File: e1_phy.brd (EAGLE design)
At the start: 100 x 75 mm, 126 parts, among them IC2 LD117AS33TR, IC3 LD117AS33TR, IC4 MCP4725, U1 IDT82V2081, U2 GPS_GNS_2201, U3 VCTCXO-CONNORWINFIELD, U4 VCXO_TAITIEN_VT, U5 IP4234CZ6, X2 SMA-142-0701-801/806, X3 JACK2.5_SJ-2523, X4 0446200002

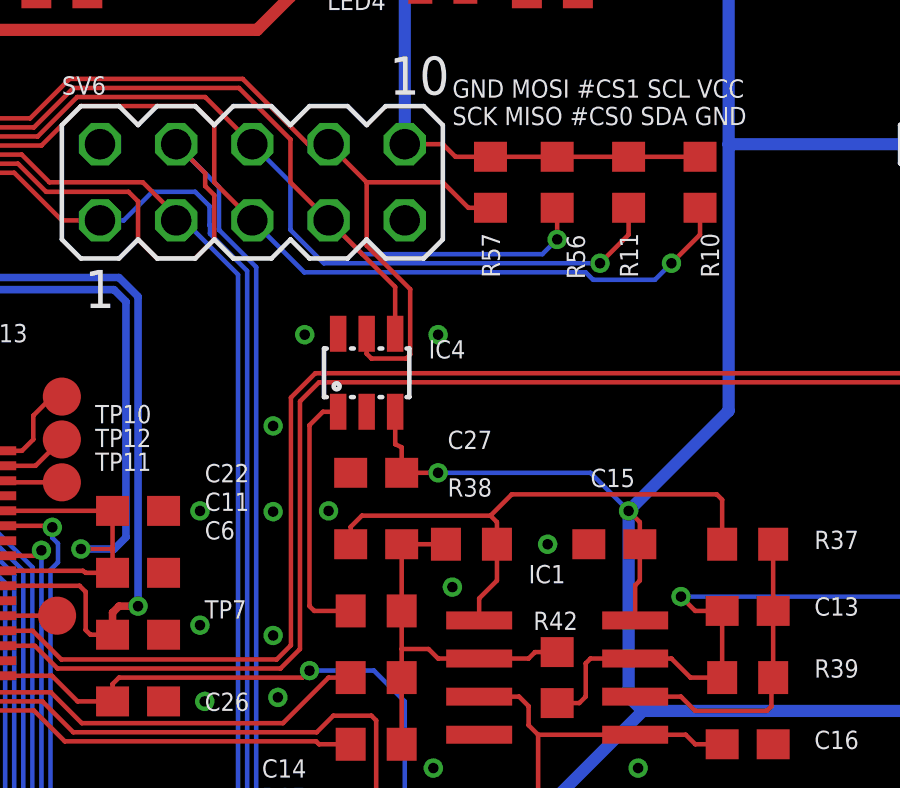
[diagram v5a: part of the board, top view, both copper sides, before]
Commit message: Implement review comments: Switch DAC to Maxim part.
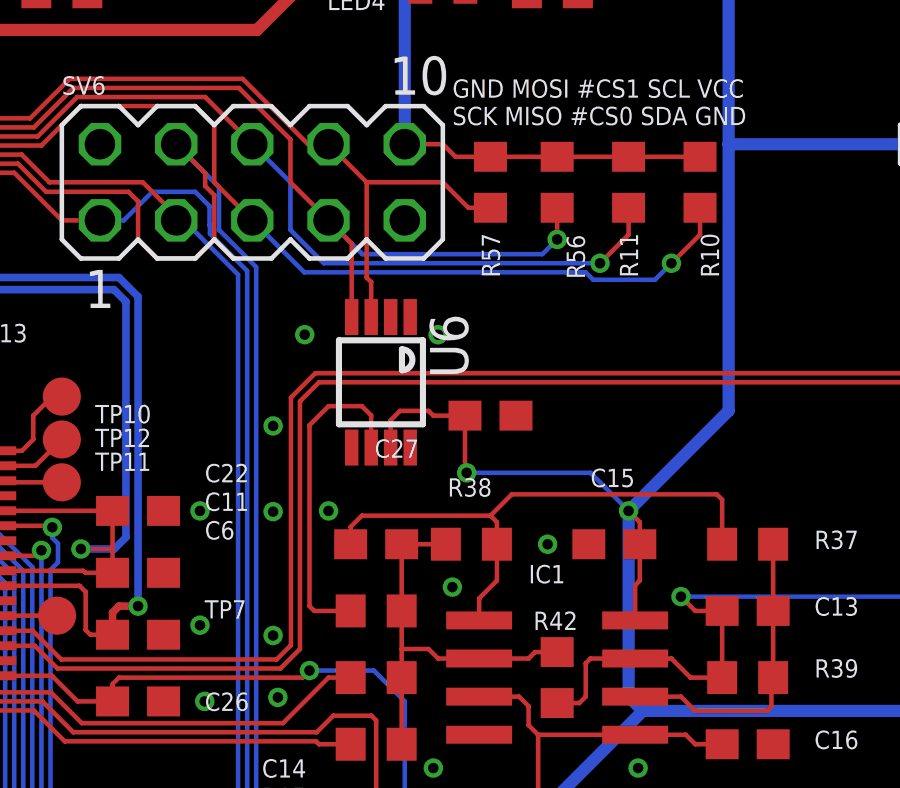
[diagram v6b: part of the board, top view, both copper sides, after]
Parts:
- removed IC4: MCP4725, dp_devices:SOT-23-6
- added U6: (no value), max5215_max5217:UMAX8
- moved C27 4.26 mm to (58.7, 44.3), turned to 180 degrees
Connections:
- net +UB: now also U6.1, U6.7; no longer IC4.3
- net DAC_I2C: now also U6.6; no longer IC4.1
- net GND: now also U6.8; no longer IC4.2, IC4.6
- net I2C_SCL: now also U6.3; no longer IC4.5
- net I2C_SDA: now also U6.4; no longer IC4.4
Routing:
- net I2C_SCL: track 53.9 -> 49.9 mm
- net DAC_I2C: track 8.61 -> 11.0 mm
- net I2C_SDA: track 59.1 -> 57.6 mm
- net +UB: track 197.5 -> 198.7 mm
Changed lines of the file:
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@@
 <attribute name="VALUE" x="25.0825" y="40.8305" size="0.0254" layer="27"/>
 </element>
-<element name="IC4" library="dp_devices" package="SOT-23-6" value="MCP4725" x="54.61" y="45.72" smashed="yes">
-<attribute name="NAME" x="56.67375" y="46.19625" size="0.6096" layer="25" font="vector" ratio="10"/>
-<attribute name="VALUE" x="53.34" y="42.2275" size="1.27" layer="27" font="vector" ratio="10"/>
-</element>
-<element name="C27" library="rcl" package="C0603" value="100n" x="54.9275" y="42.38625" smashed="yes">
-<attribute name="NAME" x="57.30875" y="43.18" size="0.6096" layer="25" font="vector"/>
-<attribute name="VALUE" x="54.2925" y="40.48125" size="1.27" layer="27"/>
+<element name="C27" library="rcl" package="C0603" value="100n" x="58.7375" y="44.29125" smashed="yes" rot="R180">
+<attribute name="NAME" x="56.35625" y="43.4975" size="0.6096" layer="25" font="vector" rot="R180"/>
+<attribute name="VALUE" x="59.3725" y="46.19625" size="1.27" layer="27" rot="R180"/>
 </element>
 <element name="R15" library="rcl" package="R0603" value="10k" x="54.9275" y="37.7825" smashed="yes">
@@
 <attribute name="OC_NEWARK" value="unknown" x="65.56375" y="22.86" size="1.778" layer="27" rot="R180" display="off"/>
 </element>
+<element name="U6" library="max5215_max5217" package="UMAX8" value="" x="55.08625" y="45.4025" rot="R180"/>
 </elements>
 <signals>
@@
 <via x="35.08375" y="39.6875" extent="1-16" drill="0.35"/>
 <contactref element="C27" pad="1"/>
-<contactref element="IC4" pad="2"/>
-<contactref element="IC4" pad="6"/>
 <contactref element="C28" pad="1"/>
 <contactref element="SV5" pad="1"/>
@@
 <contactref element="RN2" pad="4"/>
 <contactref element="RN1" pad="8"/>
+<contactref element="U6" pad="8"/>
 </signal>
 <signal name="LINE_PIN1">
@@
 <wire x1="49.2125" y1="62.865" x2="65.080875" y2="62.865" width="0.4064" layer="16"/>
 <contactref element="C27" pad="2"/>
-<contactref element="IC4" pad="3"/>
 <wire x1="63.715" y1="38.79125" x2="63.715" y2="40.005" width="0.1524" layer="1"/>
 <wire x1="63.56" y1="37.465" x2="63.56" y2="38.63625" width="0.1524" layer="1"/>
@@
 <wire x1="66.675" y1="62.540875" x2="66.675" y2="53.34" width="0.4064" layer="16"/>
 <wire x1="66.675" y1="53.34" x2="66.675" y2="44.45" width="0.4064" layer="16"/>
-<wire x1="55.56" y1="44.42" x2="55.5625" y2="44.4175" width="0.1524" layer="1"/>
-<wire x1="55.5625" y1="43.33875" x2="55.5625" y2="44.4175" width="0.1524" layer="1"/>
-<wire x1="55.7775" y1="42.38625" x2="55.7775" y2="43.23625" width="0.1524" layer="1"/>
-<wire x1="55.7775" y1="43.23625" x2="55.5625" y2="43.33875" width="0.1524" layer="1"/>
 <wire x1="84.24" y1="35.56" x2="84.24" y2="34.71" width="0.1524" layer="1"/>
 <wire x1="84.24" y1="34.71" x2="84.1375" y2="34.44875" width="0.1524" layer="1"/>
@@
 <contactref element="SV5" pad="5"/>
 <wire x1="73.66" y1="53.34" x2="66.675" y2="53.34" width="0.4064" layer="16"/>
-<wire x1="55.7775" y1="42.38625" x2="56.99125" y2="42.38625" width="0.1524" layer="1"/>
-<via x="56.99125" y="42.38625" extent="1-16" drill="0.35"/>
-<wire x1="56.99125" y1="42.38625" x2="62.07125" y2="42.38625" width="0.1524" layer="16"/>
 <wire x1="62.07125" y1="42.38625" x2="63.34125" y2="41.11625" width="0.1524" layer="16"/>
 <contactref element="U1" pad="42"/>
@@
 <wire x1="74.29105" y1="6.54890625" x2="74.29105" y2="14.3925875" width="0.254" layer="16"/>
 <wire x1="74.16925" y1="14.5143875" x2="74.16925" y2="33.21175" width="0.254" layer="16"/>
+<contactref element="U6" pad="7"/>
+<contactref element="U6" pad="1"/>
+<wire x1="55.41125" y1="43.2275" x2="55.41125" y2="44.14" width="0.1524" layer="1"/>
+<wire x1="55.72125" y1="44.45" x2="55.41125" y2="44.14" width="0.1524" layer="1"/>
+<wire x1="57.8875" y1="44.29125" x2="56.8325" y2="44.29125" width="0.1524" layer="1"/>
+<wire x1="56.8325" y1="44.29125" x2="56.67375" y2="44.45" width="0.1524" layer="1"/>
+<wire x1="56.67375" y1="44.45" x2="55.72125" y2="44.45" width="0.1524" layer="1"/>
+<wire x1="57.94375" y1="42.38625" x2="62.07125" y2="42.38625" width="0.1524" layer="16"/>
+<via x="57.94375" y="42.38625" extent="1-16" drill="0.35"/>
+<wire x1="57.94375" y1="42.38625" x2="57.8875" y2="42.4425" width="0.1524" layer="1"/>
+<wire x1="57.8875" y1="42.4425" x2="57.8875" y2="44.29125" width="0.1524" layer="1"/>
+<wire x1="55.72125" y1="44.45" x2="56.06125" y2="47.5775" width="0" layer="19" extent="1-1"/>
 </signal>
 <signal name="+UB_HALF">
@@
 <wire x1="52.07" y1="52.07" x2="53.34" y2="50.8" width="0.1524" layer="1"/>
 <wire x1="38.85385" y1="53.8995" x2="43.519175" y2="53.8995" width="0.1524" layer="1"/>
-<contactref element="IC4" pad="4"/>
-<wire x1="55.56" y1="47.02" x2="55.56" y2="47.31" width="0.1524" layer="1"/>
-<wire x1="53.34" y1="50.8" x2="55.56" y2="48.58" width="0.1524" layer="1"/>
-<wire x1="55.56" y1="48.58" x2="55.56" y2="47.02" width="0.1524" layer="1"/>
 <contactref element="R56" pad="1"/>
 <wire x1="53.34" y1="50.8" x2="54.46635" y2="49.67365" width="0.1524" layer="16"/>
@@
 <wire x1="60.96" y1="50.165" x2="60.96" y2="51.22" width="0.1524" layer="1"/>
 <wire x1="54.46635" y1="49.67365" x2="60.46865" y2="49.67365" width="0.1524" layer="16"/>
+<contactref element="U6" pad="4"/>
+<wire x1="54.11125" y1="47.5775" x2="54.11125" y2="50.02875" width="0.1524" layer="1"/>
+<wire x1="54.11125" y1="50.02875" x2="53.34" y2="50.8" width="0.1524" layer="1"/>
 </signal>
 <signal name="I2C_SCL">
@@
 <wire x1="44.7092125" y1="55.5172" x2="50.4792125" y2="55.5172" width="0.1524" layer="1"/>
 <wire x1="38.7285875" y1="54.2019" x2="43.3939125" y2="54.2019" width="0.1524" layer="1"/>
-<contactref element="IC4" pad="5"/>
 <wire x1="53.34" y1="53.34" x2="54.61" y2="52.07" width="0.1524" layer="1"/>
-<wire x1="54.61" y1="52.07" x2="54.61" y2="49.9576625" width="0.1524" layer="1"/>
-<wire x1="56.0612" y1="48.5064625" x2="56.0612" y2="46.32630625" width="0.1524" layer="1"/>
-<wire x1="54.61" y1="49.9576625" x2="56.0612" y2="48.5064625" width="0.1524" layer="1"/>
-<wire x1="55.92869375" y1="46.1938" x2="54.7712" y2="46.1938" width="0.1524" layer="1"/>
-<wire x1="56.0612" y1="46.32630625" x2="55.92869375" y2="46.1938" width="0.1524" layer="1"/>
-<wire x1="54.7712" y1="46.1938" x2="54.61" y2="46.355" width="0.1524" layer="1"/>
-<wire x1="54.61" y1="46.355" x2="54.61" y2="47.02" width="0.1524" layer="1"/>
 <contactref element="R57" pad="1"/>
 <wire x1="58.7375" y1="51.22" x2="58" y2="51.22" width="0.1524" layer="1"/>
 <wire x1="58" y1="51.22" x2="57.15" y2="52.07" width="0.1524" layer="1"/>
 <wire x1="57.15" y1="52.07" x2="54.61" y2="52.07" width="0.1524" layer="1"/>
+<contactref element="U6" pad="3"/>
+<wire x1="54.76125" y1="47.5775" x2="54.76125" y2="48.74375" width="0.1524" layer="1"/>
+<wire x1="54.76125" y1="48.74375" x2="54.61" y2="48.895" width="0.1524" layer="1"/>
+<wire x1="54.61" y1="48.895" x2="54.61" y2="52.07" width="0.1524" layer="1"/>
 </signal>
 <signal name="VCXO_EN">
@@
 <signal name="DAC_I2C">
 <contactref element="R15" pad="1"/>
-<contactref element="IC4" pad="1"/>
 <wire x1="54.0775" y1="37.7825" x2="52.86375" y2="37.7825" width="0.1524" layer="1"/>
 <wire x1="52.86375" y1="37.7825" x2="52.705" y2="37.94125" width="0.1524" layer="1"/>
-<wire x1="52.705" y1="43.97375" x2="52.705" y2="37.94125" width="0.1524" layer="1"/>
-<wire x1="53.66" y1="44.42" x2="53.15125" y2="44.42" width="0.1524" layer="1"/>
-<wire x1="53.15125" y1="44.42" x2="52.705" y2="43.97375" width="0.1524" layer="1"/>
+<wire x1="52.705" y1="37.94125" x2="52.705" y2="43.97375" width="0.1524" layer="1"/>
+<contactref element="U6" pad="6"/>
+<wire x1="52.705" y1="43.97375" x2="53.34" y2="44.60875" width="0.1524" layer="1"/>
+<wire x1="54.45125" y1="44.60875" x2="53.34" y2="44.60875" width="0.1524" layer="1"/>
+<wire x1="54.76125" y1="43.2275" x2="54.76125" y2="44.29875" width="0.1524" layer="1"/>
+<wire x1="54.76125" y1="44.29875" x2="54.45125" y2="44.60875" width="0.1524" layer="1"/>
 </signal>
 <signal name="LED1">

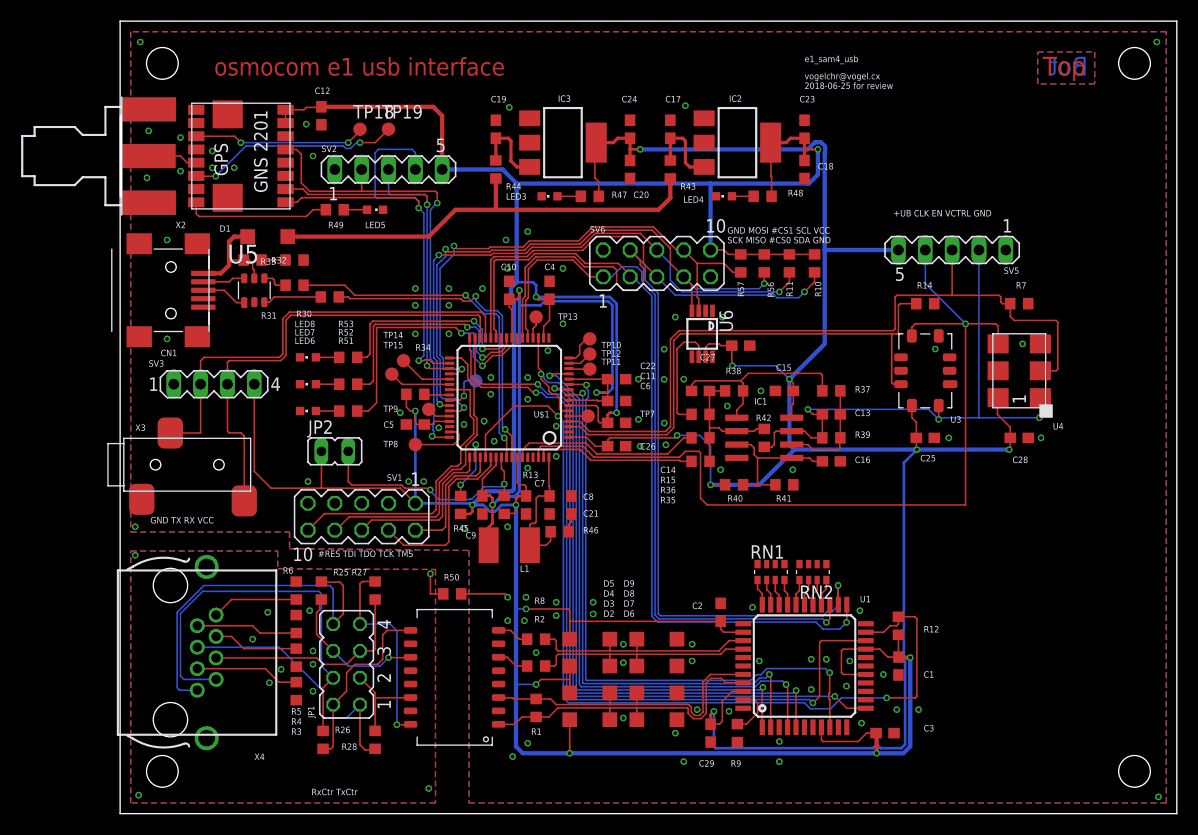
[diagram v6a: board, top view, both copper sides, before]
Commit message: More review comments implemented.
Done:
 - ESD protection on UART
 - changed JTAG to 2x10 standard ARM (but only minimal usage of pins on
	 SAM4S)
 - FTDI pinout on serial port header
 - LEDS moved near frontpanel, maybe later exchange by side-emitting
   type

Refused:
 - change R on LEDs (can change later if too dim)
 - termination on GPS rx/tx/pp
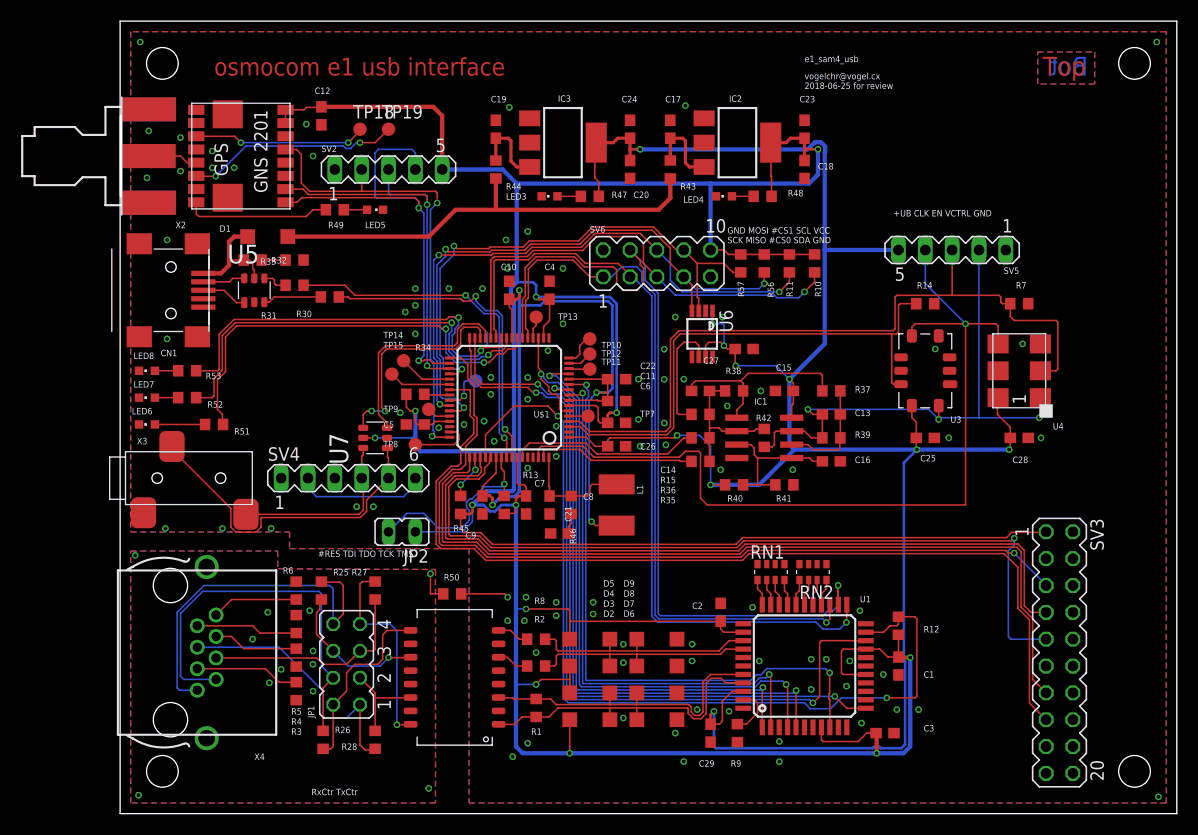
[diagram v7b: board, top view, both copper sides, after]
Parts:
- removed SV1: (no value), con-lstb:MA05-2
- added SV4: (no value), con-lstb:MA06-1
- added U7: IP4234CZ6, laforge:TSOP-6
- SV3: device con-lstb:MA04-1 -> con-lstb:MA10-2
- moved SV3 83.9 mm to (88.9, 15.2), turned to 270 degrees
- moved LED6 15.3 mm to (2.54, 36.8)
- moved LED7 15.3 mm to (2.54, 39.4)
- moved LED8 15.3 mm to (2.54, 41.9)
- moved R52 15.3 mm to (6.35, 39.4)
- moved R53 15.3 mm to (6.35, 41.9)
- moved R51 12.8 mm to (8.89, 36.8)
- moved L1 10.9 mm to (47.0, 29.2), turned to 270 degrees
- moved JP2 9.92 mm to (26.7, 26.7), turned to 90 degrees
- moved C21 2.92 mm to (41.6, 26.5), turned to 180 degrees
- moved R46 2.77 mm to (42.7, 29.2), turned to 90 degrees
- moved X3 1.28 mm to (6.51, 31.8)
- moved C27 0.45 mm to (59.1, 44.0)
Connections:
- new net N$32: SV4.2, SV4.6
- new net URXD0_SAMBA_RX_CON: SV4.4, U7.6, X3.2
- new net UTXD0_SAMBA_TX_CON: SV4.5, U7.1, X3.3
- net #RESET: now also SV3.15; no longer SV1.10
- net GND: now also SV3.10, SV3.12, SV3.14, SV3.16, SV3.18, SV3.20, SV3.4, SV3.6, SV3.8, SV4.1, U7.2; no longer SV1.3, SV1.5, SV1.9, SV3.1
- net TCK_SWDCLK: now also SV3.9; no longer SV1.4
- net TDI: now also SV3.5; no longer SV1.8
- net TDO: now also SV3.13; no longer SV1.6
- net TMS_SWDIO: now also SV3.7; no longer SV1.2
- net URXD0_SAMBA_RX: now also U7.4; no longer SV3.3, X3.2
- net UTXD0_SAMBA_TX: now also U7.3; no longer SV3.2, X3.3
- net VCC: now also SV3.1, U7.5; no longer SV1.1, SV3.4
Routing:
- net TDO: track 15.6 -> 79.8 mm
- net #RESET: track 28.2 -> 90.5 mm
- net TMS_SWDIO: track 12.1 -> 73.6 mm
- net TCK_SWDCLK: track 17.3 -> 77.8 mm, vias 0 -> 1
- net TDI: track 28.9 -> 80.8 mm, vias 0 -> 1
- net VCC: track 347.7 -> 391.0 mm, vias 11 -> 12
- net UTXD0_SAMBA_TX_CON: track 0.00 -> 31.8 mm
- net URXD0_SAMBA_RX: track 44.2 -> 21.0 mm, vias 0 -> 2
- net UTXD0_SAMBA_TX: track 42.8 -> 20.4 mm
- net LED3: track 19.8 -> 40.4 mm
- net URXD0_SAMBA_RX_CON: track 0.00 -> 17.3 mm
- net LED2: track 23.5 -> 39.9 mm
- net LED1: track 26.9 -> 41.0 mm
- net N$32: track 0.00 -> 12.5 mm
- net VDDCORE: track 66.5 -> 77.7 mm, vias 3 -> 4
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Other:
- board text removed: "GND TX RX VCC"

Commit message: Implementing further review comments:
* SPI/I2C header UEXT compatible 2x5
* Pullups on #RESET & JTAG TCK, TMS = SWDIO, SWCK
* Pullup on UART RX
* Pullup on Liu #RST
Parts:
- removed R56, R57: 10k, rcl:R0603
- added RN3, RN4: 10k, resistor-dil:EXB38V
- moved R10 49.7 mm to (18.9, 35.6)
- moved R11 46.6 mm to (77.5, 7.62), turned to 270 degrees
- moved C8 1.27 mm to (40.6, 30.5)
- moved R46 1.27 mm to (42.7, 30.5)
- moved C21 0.85 mm to (41.9, 27.3)
- moved L1 0.32 mm to (47.3, 29.2)
- renumbered SV6 to SV1
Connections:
- net #RESET: now also RN4.4
- net #RST_LIU: now also R11.1
- net #SPI_CS0: now also RN3.2, SV1.10; no longer R10.1, SV1.5
- net #SPI_CS2: now also RN3.4, SV1.4; no longer R11.1, SV1.6
- net GND: no longer SV1.9
- net I2C_SCL: now also RN3.3, SV1.5; no longer R57.1, SV1.8
- net I2C_SDA: now also RN3.1, SV1.6; no longer R56.1, SV1.7
- net SPI_MISO: now also SV1.7; no longer SV1.3
- net SPI_MOSI: now also SV1.8; no longer SV1.4
- net SPI_SCK: now also SV1.9; no longer SV1.1
- net TCK_SWDCLK: now also RN4.2
- net TMS_SWDIO: now also RN4.1
- net URXD0_SAMBA_RX_CON: now also R10.1
- net VCC: now also RN3.5, RN3.6, RN3.7, RN3.8, RN4.5, RN4.6, RN4.7, RN4.8, SV1.1; no longer R56.2, R57.2, SV1.10
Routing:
- net VCC: track 391.0 -> 424.1 mm
- net #RESET: track 90.5 -> 102.9 mm
- net I2C_SCL: track 49.9 -> 58.1 mm, vias 2 -> 3
- net TCK_SWDCLK: track 77.8 -> 85.4 mm
- net #RST_LIU: track 69.8 -> 77.3 mm
- net TMS_SWDIO: track 73.6 -> 81.0 mm
- net #SPI_CS0: track 44.0 -> 37.0 mm, vias 1 -> 0
- net SPI_SCK: track 70.4 -> 77.0 mm, vias 1 -> 2
- net SPI_MISO: track 75.5 -> 80.0 mm, vias 1 -> 2
- net I2C_SDA: track 57.6 -> 62.0 mm, vias 3 -> 4
- net URXD0_SAMBA_RX_CON: track 17.3 -> 21.4 mm
- net SPI_MOSI: track 82.2 -> 86.0 mm
- net #SPI_CS2: track 54.1 -> 51.8 mm
- net VDDPLL: track 10.9 -> 9.52 mm
- net N$15: track 1.96 -> 2.87 mm
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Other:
- board text added: "ERASE"
- board text added: "GND - - RxD TxD -"
- board text removed: "#RES TDI TDO TCK TMS"
- board text removed: "GND MOSI #CS1 SCL VCC SCK MISO #CS0 SDA GND"
